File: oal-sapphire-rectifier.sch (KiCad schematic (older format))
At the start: 10 parts, among them J1 OUTPUT, P1 IEC, P2 STAR_GROUND, SW1 Switch_DPST, T1 TALEMA-25VA/12V

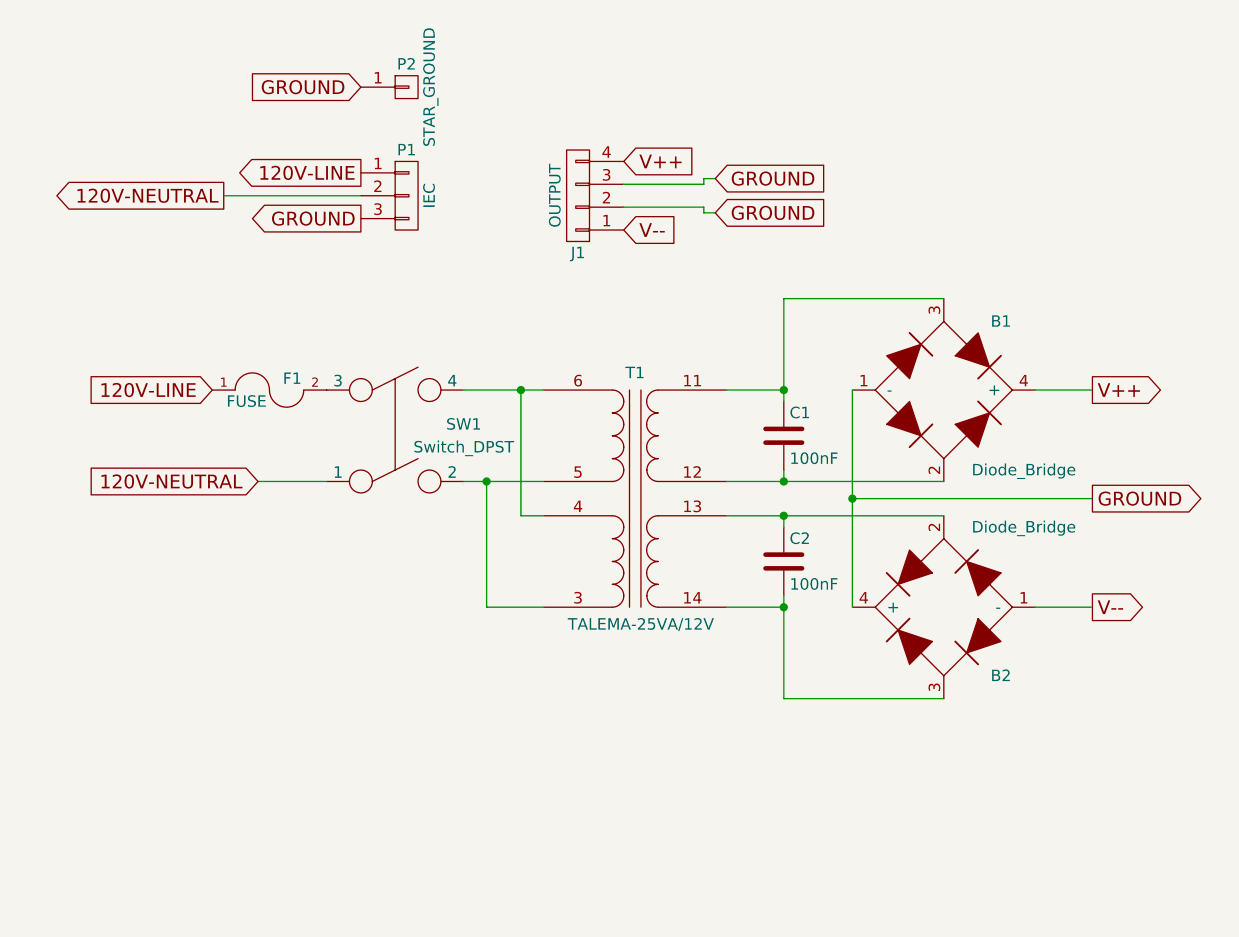
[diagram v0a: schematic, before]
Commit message: initial component placement
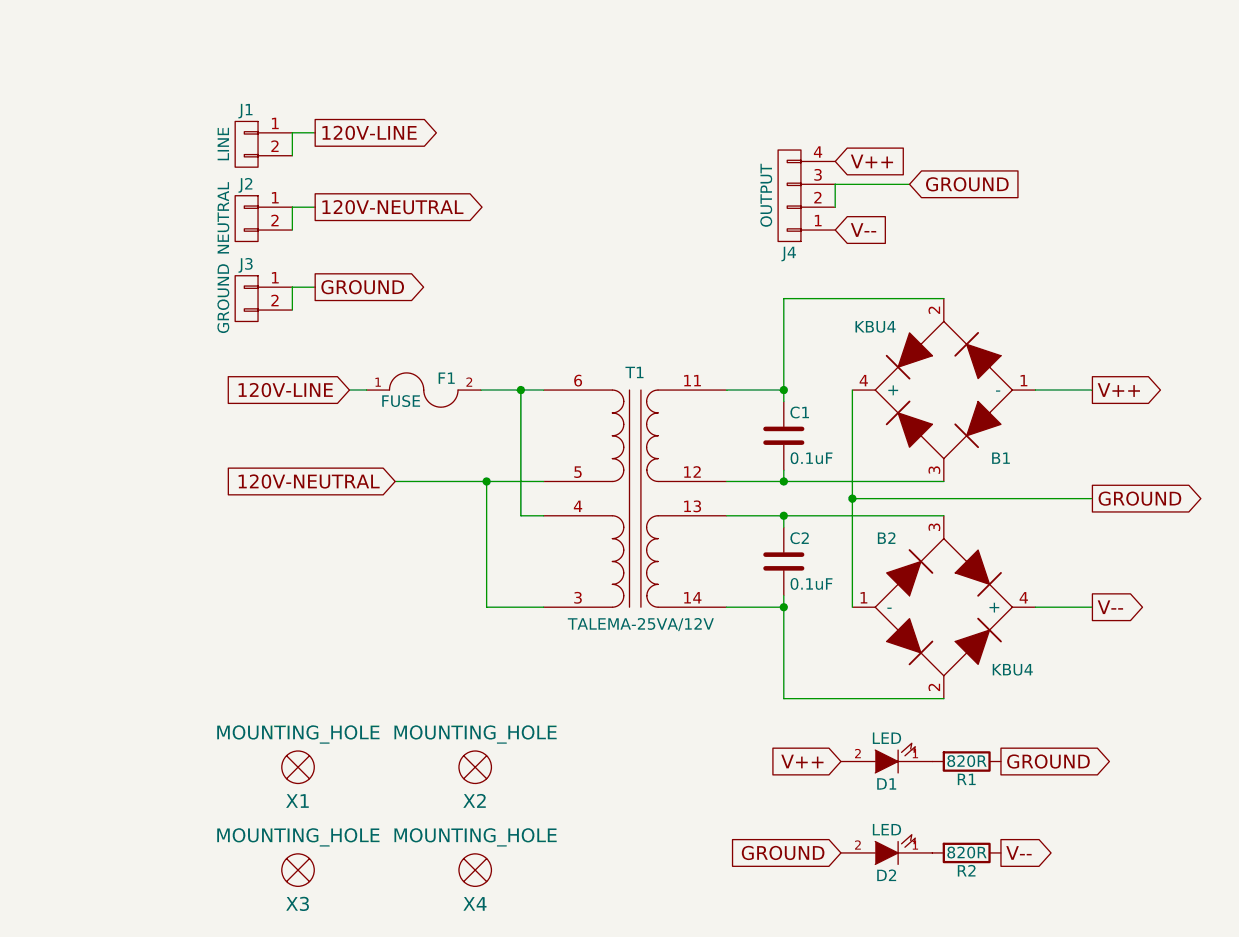
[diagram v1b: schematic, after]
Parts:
- removed P1: IEC, symbol CONN_01X03
- removed P2: STAR_GROUND, symbol CONN_01X01
- removed SW1: Switch_DPST, symbol Switch_DPST
- added D1, D2: LED, LEDs:LED-3MM, symbol LED
- added J1: LINE, ose-audio-labs:PHEONIX_SPT_5-2POS, symbol CONN_01X02
- added J2: NEUTRAL, ose-audio-labs:PHEONIX_SPT_5-2POS, symbol CONN_01X02
- added J3: GROUND, ose-audio-labs:PHEONIX_SPT_5-2POS, symbol CONN_01X02
- added R1, R2: 820R, Resistors_ThroughHole:Resistor_Horizontal_RM10mm, symbol R
- added X1, X2, X3, X4: MOUNTING_HOLE, ose-audio-labs:MOUNTING_HOLE-M3, symbol MOUNTING_HOLE
- B1, B2: value Diode_Bridge -> KBU4; footprint (none) -> ose-audio-labs:VISHAY-KBU4
- C1, C2: value 100nF -> 0.1uF
- F1: footprint (none) -> ose-audio-labs:LITTLEFUSE-560-TR5
- J4: renamed from J1; footprint (none) -> ose-audio-labs:MSTBA-2.5_4-G
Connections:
- net 120V-LINE: now also J1.1 (P1), J1.2 (P2)
- net 120V-NEUTRAL: now also T1.3 (PRIMARY2-NODOT), T1.5 (PRIMARY1-NODOT), J2.1 (P1), J2.2 (P2)
- net GROUND: now also B1.4 (+), B2.1 (-), D2.2 (A), J3.1 (P1), J3.2 (P2), R1.1; no longer B1.1 (-), B2.4 (+)
- net V++: now also B1.1 (-), D1.2 (A); no longer B1.4 (+)
- net V--: now also B2.4 (+), R2.1; no longer B2.1 (-)
- net at C1.2, T1.12 (SECONDARY1-NODOT): now also B1.3; no longer B1.2
- net at C1.1, T1.11 (SECONDARY1-DOT): now also B1.2; no longer B1.3
- net at C2.1, T1.13 (SECONDARY2-DOT): now also B2.3; no longer B2.2
- net at C2.2, T1.14 (SECONDARY2-NODOT): now also B2.2; no longer B2.3
- net at T1.4 (PRIMARY2-DOT), T1.6 (PRIMARY1-DOT): now also F1.2
- new net: D1.1 (K), R1.2
- new net: D2.1 (K), R2.2
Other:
- moved on the sheet: F1, J4
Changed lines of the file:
@@
 $EndDescr
-$Comp
-L Diode_Bridge B1
-U 1 1 56DD13B5
-P 7450 3750
-F 0 "B1" H 7700 4050 50  0000 C CNN
-F 1 "Diode_Bridge" H 7800 3400 50  0000 C CNN
-F 2 "" H 7450 3750 50  0001 C CNN
-F 3 "" H 7450 3750 50  0000 C CNN
-	1    7450 3750
-	1    0    0    -1
-$EndComp
-$Comp
-L Diode_Bridge B2
-U 1 1 56DD13F4
-P 7450 4700
-F 0 "B2" H 7200 5000 50  0000 C CNN
-F 1 "Diode_Bridge" H 7100 4350 50  0000 C CNN
-F 2 "" H 7450 4700 50  0001 C CNN
-F 3 "" H 7450 4700 50  0000 C CNN
-	1    7450 4700
-	-1   0    0    1
-$EndComp
 $Comp
 L TRANSFO_DUAL-DUAL T1
@@
 P 6750 3950
 F 0 "C1" H 6775 4050 50  0000 L CNN
-F 1 "100nF" H 6775 3850 50  0000 L CNN
+F 1 "0.1uF" H 6775 3850 50  0000 L CNN
 F 2 "ose-audio-labs:TDK-B32529-63VAC" H 6788 3800 50  0001 C CNN
 F 3 "" H 6750 3950 50  0000 C CNN
@@
 P 6750 4500
 F 0 "C2" H 6775 4600 50  0000 L CNN
-F 1 "100nF" H 6775 4400 50  0000 L CNN
+F 1 "0.1uF" H 6775 4400 50  0000 L CNN
 F 2 "ose-audio-labs:TDK-B32529-63VAC" H 6788 4350 50  0001 C CNN
 F 3 "" H 6750 4500 50  0000 C CNN
@@
 $EndComp
 $Comp
-L CONN_01X03 P1
-U 1 1 56DD164B
-P 5100 2900
-F 0 "P1" H 5100 3100 50  0000 C CNN
-F 1 "IEC" V 5200 2900 50  0000 C CNN
-F 2 "" H 5100 2900 50  0001 C CNN
-F 3 "" H 5100 2900 50  0000 C CNN
-	1    5100 2900
-	1    0    0    -1
-$EndComp
-$Comp
-L CONN_01X04 J1
+L CONN_01X04 J4
 U 1 1 56DD1690
-P 5850 2900
-F 0 "J1" H 5850 3150 50  0000 C CNN
-F 1 "OUTPUT" V 5950 2900 50  0000 C CNN
-F 2 "" H 5850 2900 50  0001 C CNN
-F 3 "" H 5850 2900 50  0000 C CNN
-	1    5850 2900
+P 6775 2900
+F 0 "J4" H 6775 3150 50  0000 C CNN
+F 1 "OUTPUT" V 6875 2900 50  0000 C CNN
+F 2 "ose-audio-labs:MSTBA-2.5_4-G" H 6775 2900 50  0001 C CNN
+F 3 "" H 6775 2900 50  0000 C CNN
+	1    6775 2900
 	-1   0    0    1
 $EndComp
@@
 L FUSE F1
 U 1 1 56DD16D4
-P 4500 3750
-F 0 "F1" H 4600 3800 50  0000 C CNN
-F 1 "FUSE" H 4400 3700 50  0000 C CNN
-F 2 "" H 4500 3750 50  0001 C CNN
-F 3 "" H 4500 3750 50  0000 C CNN
-	1    4500 3750
-	1    0    0    -1
-$EndComp
-Wire Wire Line
-	5350 3750 5700 3750
+P 5175 3750
+F 0 "F1" H 5275 3800 50  0000 C CNN
+F 1 "FUSE" H 5075 3700 50  0000 C CNN
+F 2 "ose-audio-labs:LITTLEFUSE-560-TR5" H 5175 3750 50  0001 C CNN
+F 3 "" H 5175 3750 50  0000 C CNN
+	1    5175 3750
+	1    0    0    -1
+$EndComp
+Wire Wire Line
+	5425 3750 5700 3750
 Wire Wire Line
 	5600 3750 5600 4300
@@
 Connection ~ 5600 3750
 Wire Wire Line
-	5350 4150 5700 4150
+	5050 4150 5700 4150
 Wire Wire Line
 	5450 4150 5450 4700
@@
 	5450 4700 5700 4700
 Connection ~ 5450 4150
-Text GLabel 4250 3750 0    60   Input ~ 0
+Text GLabel 4850 3750 0    60   Input ~ 0
 120V-LINE
-Text GLabel 4450 4150 0    60   Input ~ 0
+Text GLabel 5050 4150 0    60   Input ~ 0
 120V-NEUTRAL
-Text GLabel 4900 2800 0    60   Output ~ 0
+Text GLabel 4700 2625 2    60   Output ~ 0
 120V-LINE
-Text GLabel 4300 2900 0    60   Output ~ 0
+Text GLabel 4700 2950 2    60   Output ~ 0
 120V-NEUTRAL
-Text GLabel 4900 3000 0    60   Output ~ 0
-GROUND
-Wire Wire Line
-	4900 2900 4300 2900
-Wire Wire Line
-	4450 4150 4750 4150
-Text GLabel 6050 2750 2    60   Input ~ 0
+Text GLabel 6975 2750 2    60   Input ~ 0
 V++
-Text GLabel 6050 3050 2    60   Input ~ 0
+Text GLabel 6975 3050 2    60   Input ~ 0
 V--
-Text GLabel 6450 2825 2    60   Input ~ 0
-GROUND
-Text GLabel 6450 2975 2    60   Input ~ 0
-GROUND
-Wire Wire Line
-	6400 2850 6050 2850
-Wire Wire Line
-	6050 2950 6400 2950
-Wire Wire Line
-	6400 2950 6400 2975
+Text GLabel 7300 2850 2    60   Input ~ 0
+GROUND
 Wire Wire Line
 	6500 4150 7450 4150
@@
 Text GLabel 8100 4700 2    60   Output ~ 0
 V--
-Wire Wire Line
-	6400 2975 6450 2975
-Wire Wire Line
-	6450 2825 6400 2825
-Wire Wire Line
-	6400 2825 6400 2850
-$Comp
-L CONN_01X01 P2
-U 1 1 56DD2D15
-P 5100 2425
-F 0 "P2" H 5100 2525 50  0000 C CNN
-F 1 "STAR_GROUND" V 5200 2425 50  0000 C CNN
-F 2 "" H 5100 2425 50  0001 C CNN
-F 3 "" H 5100 2425 50  0000 C CNN
-	1    5100 2425
-	1    0    0    -1
-$EndComp
-Text GLabel 4900 2425 0    60   Input ~ 0
-GROUND
-$Comp
-L Switch_DPST SW1
-U 1 1 56DD3017
-P 5050 3950
-F 0 "SW1" H 5350 4000 50  0000 C CNN
-F 1 "Switch_DPST" H 5350 3900 50  0000 C CNN
-F 2 "" H 5050 3950 50  0001 C CNN
-F 3 "" H 5050 3950 50  0000 C CNN
-	1    5050 3950
-	1    0    0    -1
-$EndComp
+Text GLabel 4700 3300 2    60   Output ~ 0
+GROUND
+$Comp
+L LED D1
+U 1 1 56E44DC0
+P 7200 5375
+F 0 "D1" H 7200 5475 50  0000 C CNN
+F 1 "LED" H 7200 5275 50  0000 C CNN
+F 2 "LEDs:LED-3MM" H 7200 5375 50  0001 C CNN
+F 3 "" H 7200 5375 50  0000 C CNN
+	1    7200 5375
+	-1   0    0    1
+$EndComp
+$Comp
+L R R1
+U 1 1 56E44E46
+P 7550 5375
+F 0 "R1" V 7630 5375 50  0000 C CNN
+F 1 "820R" V 7550 5375 50  0000 C CNN
+F 2 "Resistors_ThroughHole:Resistor_Horizontal_RM10mm" V 7480 5375 50  0001 C CNN
+F 3 "" H 7550 5375 50  0000 C CNN
+	1    7550 5375
+	0    1    1    0
+$EndComp
+Text GLabel 7000 5375 0    60   Input ~ 0
+V++
+Text GLabel 7700 5375 2    60   Output ~ 0
+GROUND
+$Comp
+L CONN_01X02 J1
+U 1 1 56E46DA0
+P 4400 2675
+F 0 "J1" H 4400 2825 50  0000 C CNN
+F 1 "LINE" V 4500 2675 50  0000 C CNN
+F 2 "ose-audio-labs:PHEONIX_SPT_5-2POS" H 4400 2675 50  0001 C CNN
+F 3 "" H 4400 2675 50  0000 C CNN
+	1    4400 2675
+	-1   0    0    -1
+$EndComp
+$Comp
+L CONN_01X02 J2
+U 1 1 56E46DEE
+P 4400 3000
+F 0 "J2" H 4400 3150 50  0000 C CNN
+F 1 "NEUTRAL" V 4500 3000 50  0000 C CNN
+F 2 "ose-audio-labs:PHEONIX_SPT_5-2POS" H 4400 3000 50  0001 C CNN
+F 3 "" H 4400 3000 50  0000 C CNN
+	1    4400 3000
+	-1   0    0    -1
+$EndComp
+$Comp
+L CONN_01X02 J3
+U 1 1 56E46E41
+P 4400 3350
+F 0 "J3" H 4400 3500 50  0000 C CNN
+F 1 "GROUND" V 4500 3350 50  0000 C CNN
+F 2 "ose-audio-labs:PHEONIX_SPT_5-2POS" H 4400 3350 50  0001 C CNN
+F 3 "" H 4400 3350 50  0000 C CNN
+	1    4400 3350
+	-1   0    0    -1
+$EndComp
+$Comp
+L LED D2
+U 1 1 56E4AF62
+P 7200 5775
+F 0 "D2" H 7200 5875 50  0000 C CNN
+F 1 "LED" H 7200 5675 50  0000 C CNN
+F 2 "LEDs:LED-3MM" H 7200 5775 50  0001 C CNN
+F 3 "" H 7200 5775 50  0000 C CNN
+	1    7200 5775
+	-1   0    0    1
+$EndComp
+$Comp
+L R R2
+U 1 1 56E4AF68
+P 7550 5775
+F 0 "R2" V 7630 5775 50  0000 C CNN
+F 1 "820R" V 7550 5775 50  0000 C CNN
+F 2 "Resistors_ThroughHole:Resistor_Horizontal_RM10mm" V 7480 5775 50  0001 C CNN
+F 3 "" H 7550 5775 50  0000 C CNN
+	1    7550 5775
+	0    1    1    0
+$EndComp
+Text GLabel 7000 5775 0    60   Input ~ 0
+GROUND
+Text GLabel 7700 5775 2    60   Output ~ 0
+V--
+Wire Wire Line
+	4600 2625 4600 2725
+Wire Wire Line
+	4700 2625 4600 2625
+Wire Wire Line
+	4700 2950 4600 2950
+Wire Wire Line
+	4600 2950 4600 3050
+Wire Wire Line
+	4700 3300 4600 3300
+Wire Wire Line
+	4600 3300 4600 3400
+Wire Wire Line
+	6975 2850 6975 2950
+Wire Wire Line
+	6975 2850 7300 2850
+Wire Wire Line
+	4925 3750 4850 3750
+$Comp
+L Diode_Bridge B1
+U 1 1 56E4CE8E
+P 7450 3750
+F 0 "B1" H 7200 4050 50  0000 C CNN
+F 1 "KBU4" H 7750 3475 50  0000 C CNN
+F 2 "ose-audio-labs:VISHAY-KBU4" H 7450 3750 50  0001 C CNN
+F 3 "" H 7450 3750 50  0000 C CNN
+	1    7450 3750
+	-1   0    0    1
+$EndComp
+$Comp
+L Diode_Bridge B2
+U 1 1 56E4CEE8
+P 7450 4700
+F 0 "B2" H 7200 5000 50  0000 C CNN
+F 1 "KBU4" H 7750 4425 50  0000 C CNN
+F 2 "ose-audio-labs:VISHAY-KBU4" H 7450 4700 50  0001 C CNN
+F 3 "" H 7450 4700 50  0000 C CNN
+	1    7450 4700
+	1    0    0    -1
+$EndComp
+$Comp
+L MOUNTING_HOLE X1
+U 1 1 56E4D771
+P 4625 5400
+F 0 "X1" H 4625 5250 60  0000 C CNN
+F 1 "MOUNTING_HOLE" H 4625 5550 60  0000 C CNN
+F 2 "ose-audio-labs:MOUNTING_HOLE-M3" H 4625 5400 60  0001 C CNN
+F 3 "" H 4625 5400 60  0000 C CNN
+	1    4625 5400
+	1    0    0    -1
+$EndComp
+$Comp
+L MOUNTING_HOLE X2
+U 1 1 56E4D7CC
+P 5400 5400
+F 0 "X2" H 5400 5250 60  0000 C CNN
+F 1 "MOUNTING_HOLE" H 5400 5550 60  0000 C CNN
+F 2 "ose-audio-labs:MOUNTING_HOLE-M3" H 5400 5400 60  0001 C CNN
+F 3 "" H 5400 5400 60  0000 C CNN
+	1    5400 5400
+	1    0    0    -1
+$EndComp
+$Comp
+L MOUNTING_HOLE X3
+U 1 1 56E4D82C
+P 4625 5850
+F 0 "X3" H 4625 5700 60  0000 C CNN
+F 1 "MOUNTING_HOLE" H 4625 6000 60  0000 C CNN
+F 2 "ose-audio-labs:MOUNTING_HOLE-M3" H 4625 5850 60  0001 C CNN
+F 3 "" H 4625 5850 60  0000 C CNN
+	1    4625 5850
+	1    0    0    -1
+$EndComp
+$Comp
+L MOUNTING_HOLE X4
+U 1 1 56E4D896
+P 5400 5850
+F 0 "X4" H 5400 5700 60  0000 C CNN
+F 1 "MOUNTING_HOLE" H 5400 6000 60  0000 C CNN
+F 2 "ose-audio-labs:MOUNTING_HOLE-M3" H 5400 5850 60  0001 C CNN
+F 3 "" H 5400 5850 60  0000 C CNN
+	1    5400 5850
+	1    0    0    -1
+$EndComp
